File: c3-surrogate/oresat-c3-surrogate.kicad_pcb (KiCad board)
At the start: 2 copper layers, 99.8 x 94.6 mm, 62 parts, among them J1 J-SAMTEC-TFM-120-X1-XXX-D-RA, J2 Conn_01x04, J3 Terminal Block, J4 Barrel Jack, J5 Header, J6 Header, Q1 PMV45EN, Q2 DMP3050LVT-7, Q3 PMV45EN, Q4 DMP3050LVT-7, SW1 Slide Switch, SW2 Slide Switch, U1 Trinket-M0, U2 Seeed-USB-to-UART, U3 MAX892LEUA+T

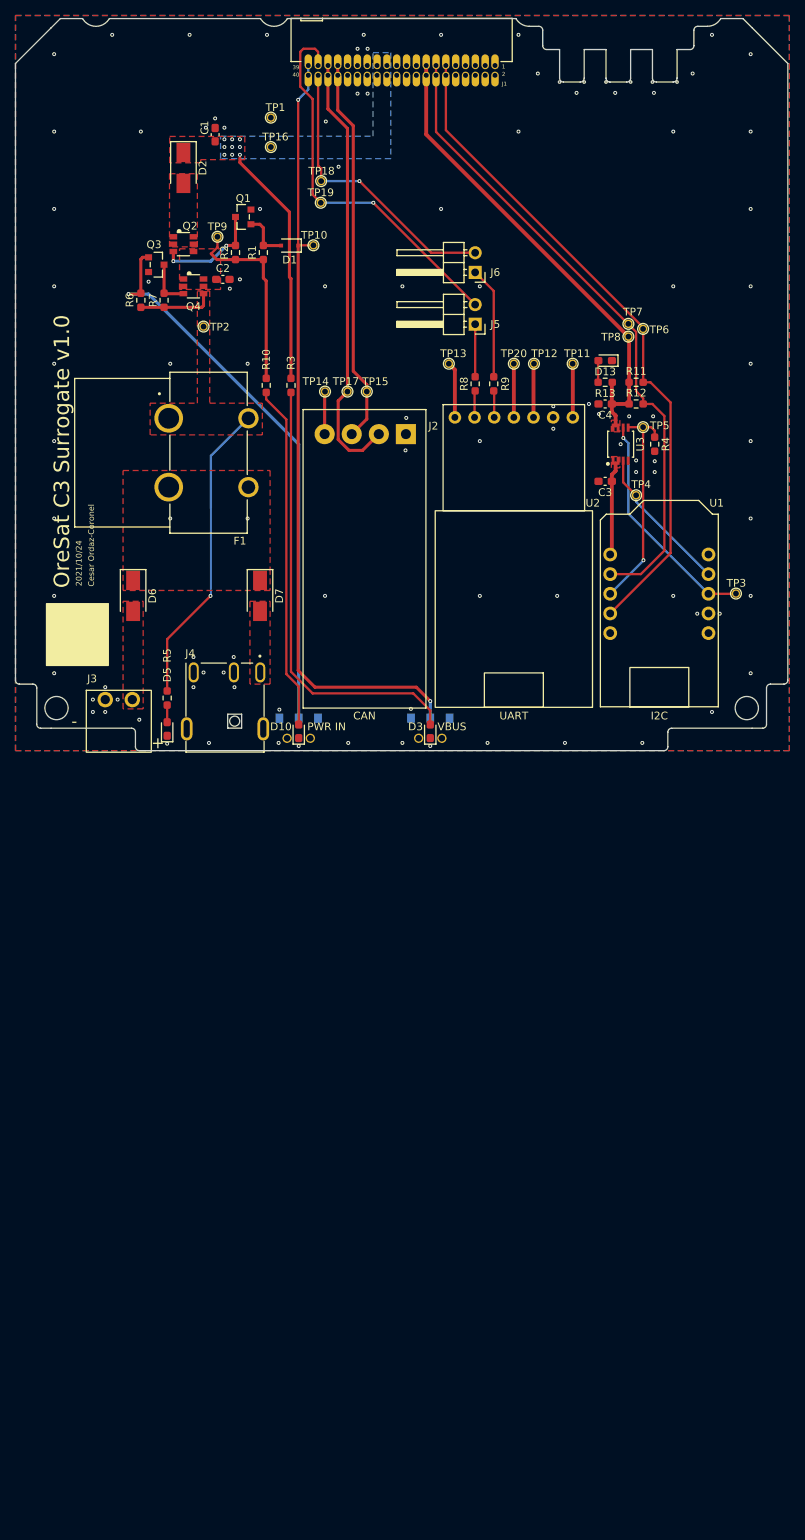
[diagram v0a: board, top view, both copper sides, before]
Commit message: updated c3 schematic
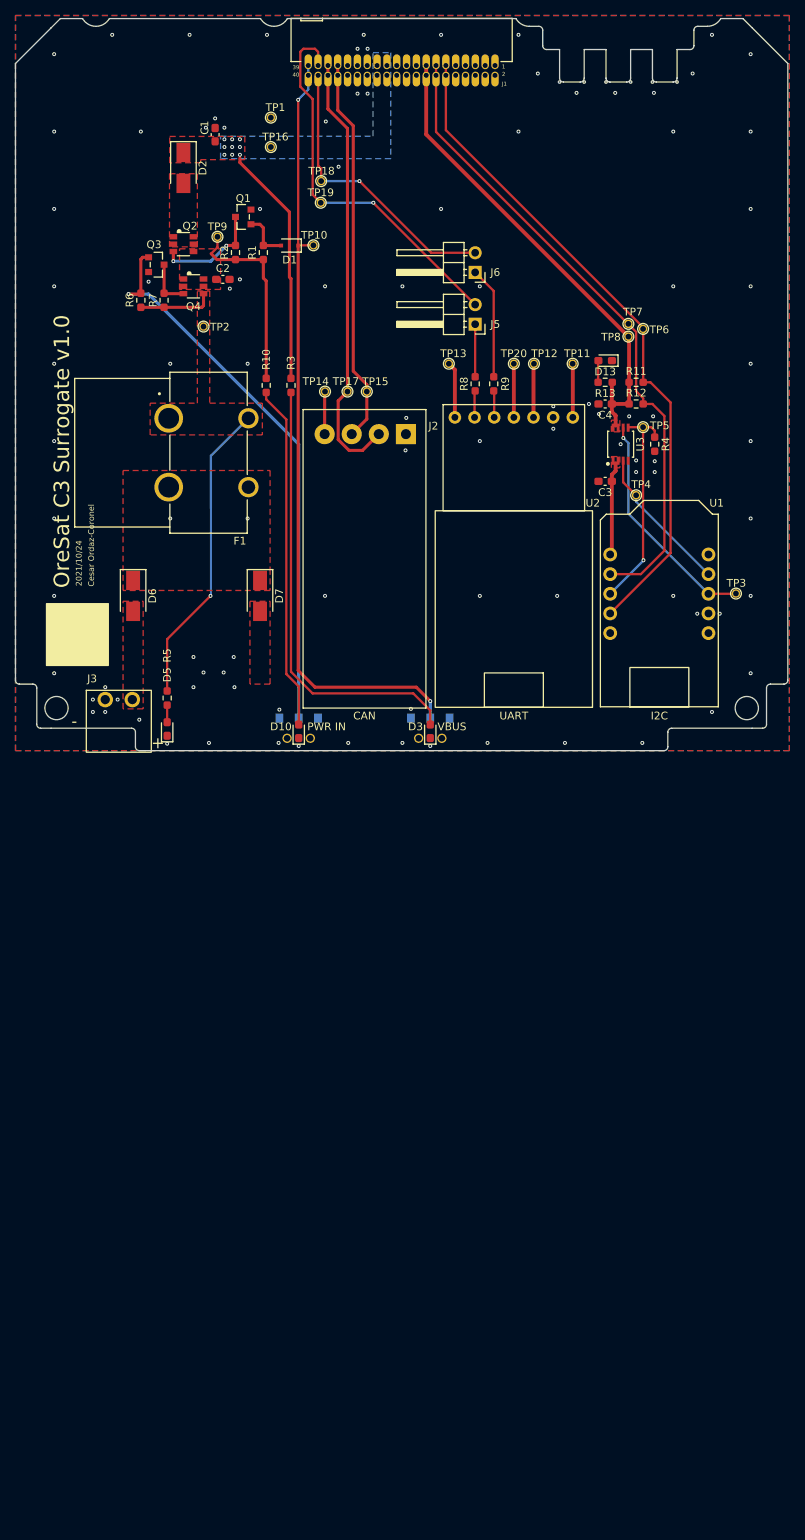
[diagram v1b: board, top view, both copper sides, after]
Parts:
- removed J4: Barrel Jack, J-CUI-PJ-051AH-Barrel-Jack:CUI_PJ-051AH

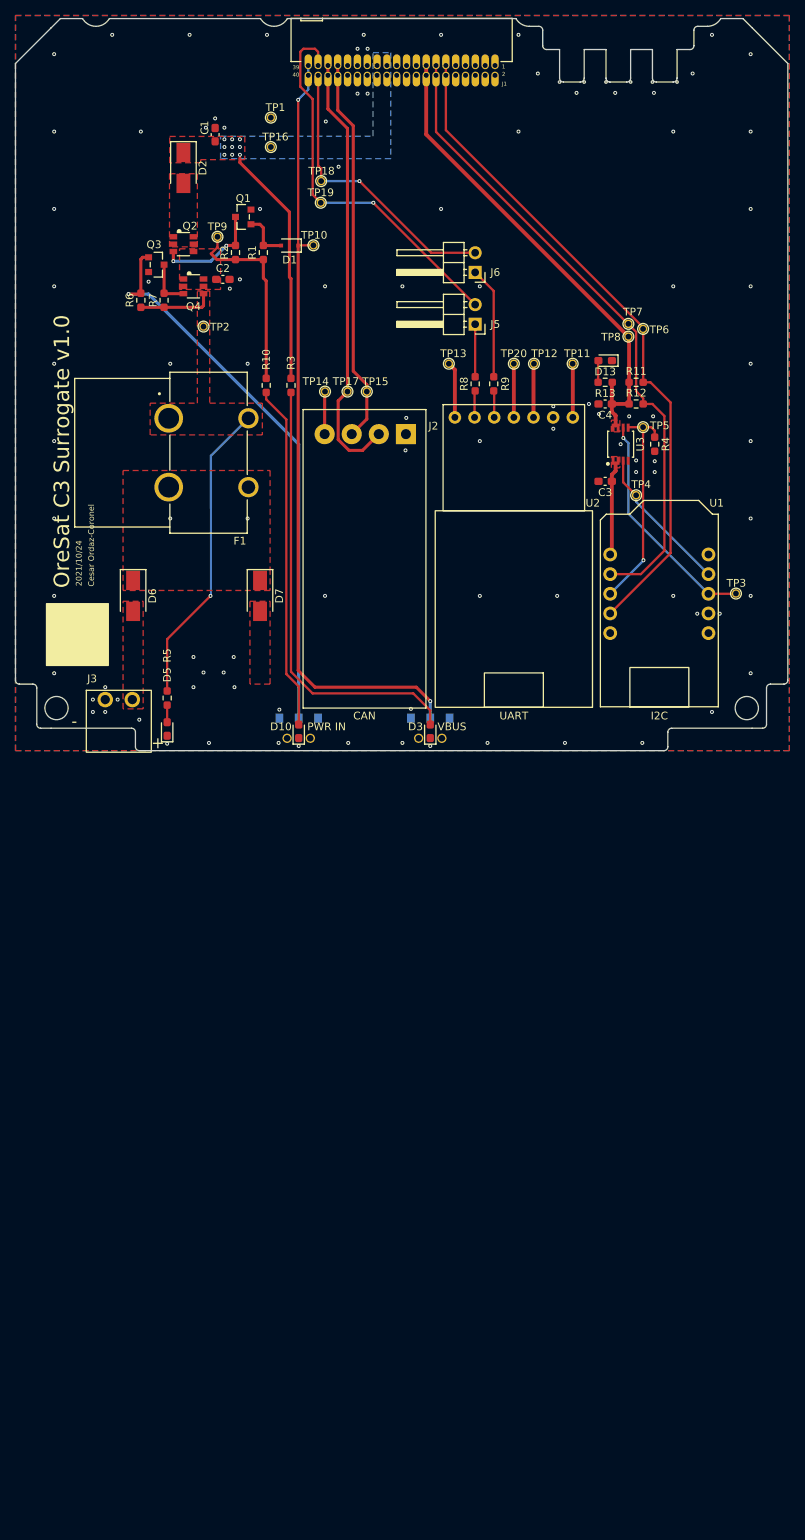
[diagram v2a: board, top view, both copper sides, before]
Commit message: modified pcb using updated schematic
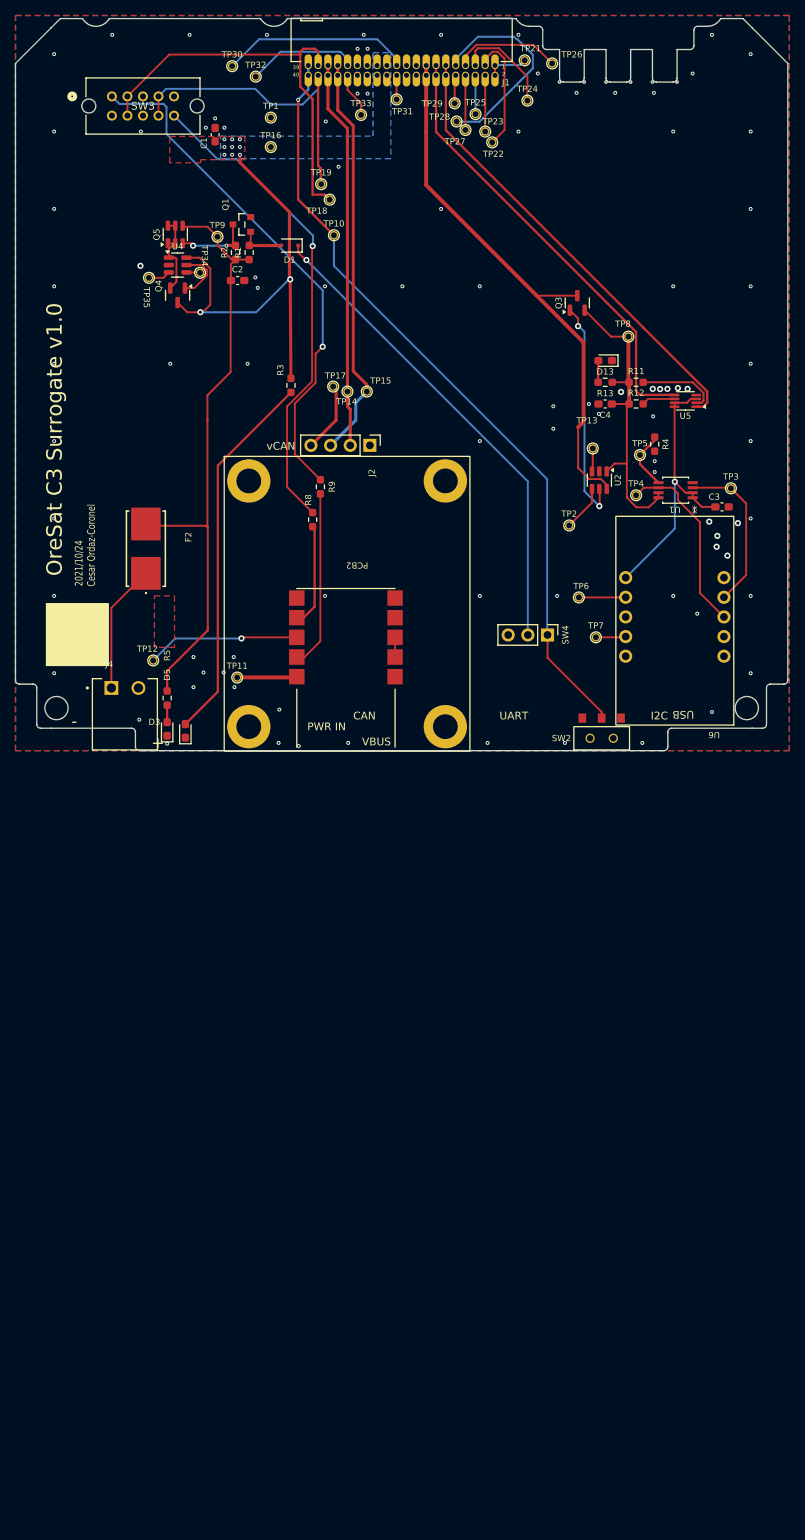
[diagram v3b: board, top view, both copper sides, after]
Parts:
- removed D10: Green, LED_SMD:LED_0603_1608Metric_Pad1.05x0.95mm_HandSolder
- removed D2, D6, D7: Schottky, Diode_SMD:D_SMA
- removed F1: ATC Fuse, F-Keystone-3550-2-ATC-Fuse-Holder:FUSE_3550-2
- removed J3: Terminal Block, J-Phoenix-2-Position-3-5mm-Terminal-Block-Header:1995499
- removed J5, J6: Header, Connector_PinHeader_2.54mm:PinHeader_1x02_P2.54mm_Horizontal
- removed Q2: DMP3050LVT-7, Mosfets:SOT23-6
- removed R10, R6, R7: 10k, Resistor_SMD:R_0603_1608Metric_Pad0.98x0.95mm_HandSolder
- removed SW1: Slide Switch, S-CK-AYZ0102AGRLC-Slide-Switch:AYZ0102AGRLC
- removed TP20: TEST-POINT-LARGE-SQUARE, oresat-misc:1X01
- removed U3: MAX892LEUA+T, U-Maxim-MAX892LEUA+T-power-switch:MAX892LEUA+T
- added F2: Fuse_Small, oresat-passives:Littelfuse 155900DR, F.Cu at (116.8, 123.9)
- added J4: Conn_01x02_Socket, oresat-connectors:PHOENIX_1995499, F.Cu at (109.9, 149.9)
- added PCB2: UMFT234XF, oresat-misc:UMFT234XF, F.Cu at (149.1, 150.1)
- added Q5: DMP3050LVT-7, Package_TO_SOT_SMD:SOT-23-6, F.Cu at (120.7, 83.3)
- added SW3: OS203011MV9QS1, oresat-passives:DP3T_OS203011MV9QS1_CNK, F.Cu at (112.5, 65.5)
- added SW4: EG1218, Connector_PinHeader_2.54mm:PinHeader_1x03_P2.54mm_Vertical, F.Cu at (168.8, 135.1)
- added TP21: Test-Point, oresat-misc:TestPoint-0.75mm-th, F.Cu at (165.8, 60.8)
- added TP22: Test-Point, oresat-misc:TestPoint-0.75mm-th, F.Cu at (161.6, 71.4)
- added TP23: Test-Point, oresat-misc:TestPoint-0.75mm-th, F.Cu at (160.7, 70.0)
- added TP24: Test-Point, oresat-misc:TestPoint-0.75mm-th, F.Cu at (166.2, 66.0)
- added TP25: Test-Point, oresat-misc:TestPoint-0.75mm-th, F.Cu at (159.4, 67.8)
- added TP26: Test-Point, oresat-misc:TestPoint-0.75mm-th, F.Cu at (169.3, 61.2)
- added TP27: Test-Point, oresat-misc:TestPoint-0.75mm-th, F.Cu at (158.2, 69.8)
- added TP28: Test-Point, oresat-misc:TestPoint-0.75mm-th, F.Cu at (157.0, 68.7)
- added TP29: Test-Point, oresat-misc:TestPoint-0.75mm-th, F.Cu at (156.8, 66.3)
- added TP30: Test-Point, oresat-misc:TestPoint-0.75mm-th, F.Cu at (128.0, 61.5)
- added TP31: Test-Point, oresat-misc:TestPoint-0.75mm-th, F.Cu at (149.2, 65.8)
- added TP32: Test-Point, oresat-misc:TestPoint-0.75mm-th, F.Cu at (131.1, 62.9)
- added TP33: Test-Point, oresat-misc:TestPoint-0.75mm-th, F.Cu at (144.7, 67.8)
- added TP34: Test-Point, oresat-misc:TestPoint-0.75mm-th, F.Cu at (123.8, 88.2)
- added TP35: Test-Point, oresat-misc:TestPoint-0.75mm-th, F.Cu at (117.2, 88.9)
- added U4: LTC4412xS6, Package_TO_SOT_SMD:TSOT-23-6, F.Cu at (121.0, 87.2)
- added U5: TS5A21366, Package_SO:VSSOP-8_2.3x2mm_P0.5mm, F.Cu at (186.6, 104.8)
- added U6: Trinket-M0, oresat-mcu:Adafruit-Trinket, F.Cu at (185.2, 132.7)
- added vCAN: vulCAN, oresat-pcbs:vulCAN, F.Cu at (130.2, 115.2)
- J2: footprint TerminalBlock_4Ucon:TerminalBlock_4Ucon_1x04_P3.50mm_Vertical -> Connector_PinHeader_2.54mm:PinHeader_1x04_P2.54mm_Vertical
- Q1: footprint Mosfets:SOT23-3 -> oresat-ics:SOT23
- Q3: value PMV45EN -> NTR2101P; footprint Mosfets:SOT23-3 -> Package_TO_SOT_SMD:SOT-23
- Q4: value DMP3050LVT-7 -> NTR2101P; footprint Mosfets:SOT23-6 -> Package_TO_SOT_SMD:SOT-23
- R8, R9: value 10k -> 100
- SW2: moved to F.Cu
- TP1, TP10, TP11, TP12, TP13, TP14, TP15, TP16, TP17, TP18, TP19, TP2, TP3, TP4, TP5, TP6, TP7, TP8, TP9: value TEST-POINT-LARGE-SQUARE -> Test-Point; footprint oresat-misc:1X01 -> oresat-misc:TestPoint-0.75mm-th
- U1: value Trinket-M0 -> MAX892LEUA+T; footprint Adafruit-Trinket-M0:Trinket-M0 -> oresat-passives:MAX892
- U2: value Seeed-USB-to-UART -> LTC4412xS6; footprint Seeed-USB-to-UART:Seeed-USB-to-UART -> Package_TO_SOT_SMD:TSOT-23-6
- moved TP12 62.4 mm to (117.8, 138.3)
- moved TP11 59.4 mm to (128.7, 140.6)
- moved Q3 54.6 mm to (172.6, 92.2), turned to 90 degrees
- moved TP2 53.8 mm to (171.6, 120.9)
- moved TP7 40.7 mm to (175.0, 135.3)
- moved TP6 35.7 mm to (172.8, 130.2)
- moved D3 31.7 mm to (122.0, 147.4)
- moved R8 27.4 mm to (138.4, 120.2)
- moved R9 26.1 mm to (139.4, 115.9)
- moved SW2 22.2 mm to (175.8, 148.4), turned to 0 degrees
- moved TP13 21.6 mm to (174.6, 111.0)
- moved U2 20.0 mm to (175.4, 115.0), turned to -90 degrees
- moved C3 15.5 mm to (191.3, 118.5), turned to 0 degrees
- moved U1 14.8 mm to (185.3, 116.3)
- moved TP3 13.6 mm to (192.4, 116.1)
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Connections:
- C2 pad 1: Net-(C2-Pad1) -> Net-(Q5-S)
- C3 pad 1: Net-(C3-Pad1) -> Net-(U1-IN)
- C4 pad 1: OPD_PWR -> Net-(Q3-S)
- D1 pad 1: /~{SD} -> Net-(D1-K)
- Q3 pad 1: Net-(Q3-Pad1) -> Net-(Q3-G)
- Q3 pad 2: GND -> Net-(Q3-S)
- Q3 pad 3: Net-(Q3-Pad3) -> OPD_PWR
- Q4 pad 1: Net-(C2-Pad1) -> Net-(Q4-G)
- Q4 pad 2: Net-(C2-Pad1) -> Net-(Q4-S)
- Q4 pad 3: Net-(Q3-Pad3) -> VBUS
- R1 pad 1: Net-(C2-Pad1) -> Net-(Q5-S)
- R11 pad 1: OPD_PWR -> Net-(Q3-S)
- R11 pad 2: OPD_SDA -> Net-(U5-COM1)
- R12 pad 1: OPD_PWR -> Net-(Q3-S)
- R12 pad 2: OPD_SCL -> Net-(U5-COM2)
- R13 pad 1: OPD_PWR -> Net-(Q3-S)
- R2 pad 1: Net-(C2-Pad1) -> Net-(Q5-S)
- R5 pad 1: Net-(F1-Pad1_1) -> Net-(Q5-S)
- R8 pad 1: Net-(R8-Pad1) -> Net-(PCB2-TXD)
- R9 pad 1: Net-(R9-Pad1) -> Net-(PCB2-RXD)
- TP11 pad 1: Net-(TP11-Pad1) -> Net-(PCB2-CTS#)
- TP12 pad 1: Net-(TP12-Pad1) -> Net-(PCB2-RTS#)
- TP13 pad 1: Net-(TP13-Pad1) -> Net-(U2-CTL)
- TP18 pad 1: C3-UART-RX -> C3-UART-TX
- TP19 pad 1: C3-UART-TX -> C3-UART-RX
- TP2 pad 1: Net-(F1-Pad1_1) -> Net-(U2-STAT)
- TP3 pad 1: /OPD_~{FAULT} -> /OPD_~{ENABLE}
- TP4 pad 1: /OPD_~{ENABLE} -> /OPD_~{FAULT}
- TP6 pad 1: OPD_SDA -> Net-(U6-SCL)
- TP7 pad 1: OPD_SCL -> Net-(U6-SDA)
- TP8 pad 1: OPD_PWR -> Net-(Q3-S)
- TP9 pad 1: Net-(C2-Pad1) -> Net-(Q5-S)
- U1 pad 1: unconnected-(U1-Pad1) -> Net-(U1-IN)
- U1 pad 2: GND -> Net-(U1-IN)
- U1 pad 3: /OPD_~{FAULT} -> /OPD_~{ENABLE}
- U1 pad 4: /OPD_~{ENABLE} -> GND
- U1 pad 5: unconnected-(U1-Pad5) -> /OPD_ISET
- U1 pad 6: Net-(C3-Pad1) -> /OPD_~{FAULT}
- U1 pad 7: OPD_SCL -> Net-(Q3-S)
- U1 pad 8: /OPD_ISET -> Net-(Q3-S)
- U2 pad 1: Net-(TP13-Pad1) -> Net-(Q3-S)
- U2 pad 2: Net-(R8-Pad1) -> GND
- U2 pad 3: Net-(R9-Pad1) -> Net-(U2-CTL)
- U2 pad 4: Net-(TP20-Pad1) -> Net-(U2-STAT)
- U2 pad 5: Net-(TP12-Pad1) -> Net-(Q3-G)
- U2 pad 6: GND -> OPD_PWR
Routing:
- net Net-(Q5-S): track 0.00 -> 78.5 mm
- net Net-(Q3-Pad1): track 72.6 -> 0.00 mm, vias 1 -> 0
- net Net-(D1-K): track 0.00 -> 62.8 mm, vias 0 -> 1
- net Net-(R8-Pad2): track 6.79 -> 62.9 mm, vias 0 -> 1
- net Net-(R9-Pad2): track 14.5 -> 67.0 mm, vias 0 -> 1
- net Net-(F1-Pad1_1): track 49.3 -> 0.00 mm, vias 1 -> 0
- net Net-(D10-Pad2): track 44.7 -> 0.00 mm
- net Net-(Q3-S): track 0.00 -> 41.3 mm
- net Net-(U1-IN): track 0.00 -> 35.2 mm, vias 0 -> 1
- net Net-(Q3-G): track 0.00 -> 29.4 mm, vias 0 -> 2
- net /SPARE9: track 0.00 -> 27.4 mm
- net OPD_SDA: track 86.6 -> 59.2 mm
- net VBUS: track 31.2 -> 58.6 mm, vias 9 -> 11
- net OPD_SCL: track 83.9 -> 58.0 mm
- net Net-(C2-Pad1): track 25.1 -> 0.00 mm
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- added copper zone on F.Cu, net (none)
- removed copper zone on F.Cu, net Net-(C2-Pad1)
- removed copper zone on F.Cu, net Net-(C3-Pad1)
- removed copper zone on F.Cu, net Net-(D2-Pad2)
- removed copper zone on F.Cu, net Net-(D6-Pad1)
- removed copper zone on F.Cu, net Net-(D6-Pad2)
- removed copper zone on F.Cu, net Net-(D7-Pad2)
- removed copper zone on F.Cu, net Net-(F1-Pad1_1)
- removed copper zone on F.Cu, net OPD_PWR

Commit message: PCB edits
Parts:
- removed vCAN: vulCAN, oresat-pcbs:vulCAN
- added TP20: Test-Point, oresat-misc:TestPoint-0.75mm-th, F.Cu at (151.8, 68.2)
- added TP36: Test-Point, oresat-misc:TestPoint-0.75mm-th, F.Cu at (150.5, 69.8)
- moved SW3 81.0 mm to (165.2, 127.0), turned to 90 degrees
- moved TP29 24.9 mm to (181.2, 70.7)
- moved TP28 22.1 mm to (179.0, 70.7)
- moved TP27 18.7 mm to (176.8, 70.7)
- moved R9 15.8 mm to (154.1, 121.6)
- moved TP25 13.7 mm to (172.8, 70.7)
- moved R8 13.1 mm to (150.1, 126.1), turned to 0 degrees
- moved TP12 12.0 mm to (129.4, 135.3)
- moved TP26 10.9 mm to (174.8, 70.7)
- moved TP21 9.86 mm to (165.3, 70.7)
- moved TP23 8.38 mm to (169.1, 70.7)
- moved TP24 6.58 mm to (170.8, 70.7)
- moved TP22 5.80 mm to (167.3, 70.7)
- moved TP15 5.10 mm to (144.4, 98.6)
- moved TP17 5.01 mm to (142.6, 98.6)
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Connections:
- SW3 pad 1: Net-(R9-Pad2) -> unconnected-(SW3-Pad1)
- SW3 pad 2: C3-UART-TX -> C3-UART-RX
- SW3 pad 4: C3-UART-RX -> C3-UART-TX
- SW3 pad 5: unconnected-(SW3-Pad5) -> Net-(R9-Pad2)
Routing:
- net Net-(R9-Pad2): track 67.0 -> 11.8 mm, vias 1 -> 0
- net Net-(R8-Pad2): track 62.9 -> 19.6 mm, vias 1 -> 0
- net C3-UART-RX: track 41.2 -> 75.2 mm
- net C3-UART-TX: track 53.0 -> 83.5 mm
- net /SPARE10: track 3.67 -> 33.5 mm
- net /OPD_ISET: track 7.66 -> 28.5 mm
- net /SPARE8: track 7.07 -> 26.3 mm
- net /SPARE6: track 5.03 -> 22.3 mm
- net Net-(PCB2-RTS#): track 19.8 -> 7.01 mm, vias 1 -> 0
- net /SPARE7: track 14.0 -> 25.8 mm
- net OPD_PWR: track 71.1 -> 79.6 mm
- net /CAN2_L: track 0.00 -> 8.30 mm
- net /SPARE4: track 7.27 -> 15.2 mm
- net /SPARE1: track 5.38 -> 12.4 mm
- net /CAN2_H: track 0.00 -> 6.79 mm
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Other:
- board text added: "need to add vulCAN footprint"

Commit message: more pcb changes
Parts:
- moved TP2 11.8 mm to (177.5, 107.7)
- moved TP14 6.54 mm to (138.3, 104.6)
- moved U2 5.24 mm to (174.5, 109.9), turned to 90 degrees
- moved TP13 2.91 mm to (177.5, 110.8)
- moved TP3 2.21 mm to (190.2, 116.0)
- moved R3 1.96 mm to (133.7, 103.3)
- moved D1 1.83 mm to (133.6, 84.7)
- moved R13 1.61 mm to (176.4, 100.8)
- moved D13 1.50 mm to (176.2, 98.1)
- moved TP5 1.46 mm to (180.2, 110.5)
- moved R11 1.40 mm to (180.2, 101.0)
- moved TP9 1.02 mm to (126.3, 82.6)
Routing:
- net OPD_PWR: track 79.6 -> 61.1 mm
- net Net-(Q3-G): track 29.4 -> 16.9 mm, vias 2 -> 0
- net VBUS: track 58.6 -> 51.0 mm
- net /CANable_5V: track 10.9 -> 3.81 mm
- net Net-(Q4-S): track 11.4 -> 7.22 mm
- net Net-(Q3-S): track 41.3 -> 45.2 mm
- net /OPD_~{ENABLE}: track 21.1 -> 17.5 mm
- net Net-(D1-A): track 6.31 -> 4.48 mm
- net /OPD_ISET: track 28.5 -> 29.9 mm
- net Net-(D3-A): track 48.5 -> 47.2 mm
- net /~{SD}: track 103.3 -> 102.2 mm
- net Net-(U5-COM1): track 10.4 -> 11.3 mm
- net Net-(U2-CTL): track 3.00 -> 2.17 mm
- net Net-(Q4-G): track 7.12 -> 7.91 mm
- net Net-(Q5-S): track 78.3 -> 79.0 mm
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- added copper zone on F.Cu, net Net-(Q4-S)
